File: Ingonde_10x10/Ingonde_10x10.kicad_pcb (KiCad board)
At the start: 2 copper layers, 100 x 100 mm, 738 parts, among them J1 2060-451/998-404, J10 2060-451/998-404, J100 Pastille, J101 Pastille, J102 Pastille, J103 Pastille, J104 Pastille, J105 Pastille, J106 Pastille, J107 Pastille, J108 Pastille, J109 Pastille, J11 2060-451/998-404, J110 Pastille, J111 Pastille, J112 Pastille, J113 Pastille, J114 Pastille, J115 Pastille, J116 Pastille, J117 Pastille, J118 Pastille, J119 Pastille, J12 2060-451/998-404, J120 Pastille, J121 Pastille, J122 Pastille, J123 Pastille, J124 Pastille, J125 Pastille, J126 Pastille, J127 Pastille, J128 Pastille, J129 Pastille, J13 2060-451/998-404, J130 Pastille, J131 Pastille, J132 Pastille, J133 Pastille, J134 Pastille, J135 Pastille, J136 Pastille, J137 Pastille, J138 Pastille, J139 Pastille, J14 2060-451/998-404, J140 Pastille, J141 Pastille, J142 Pastille, J143 Pastille, J144 Pastille, J145 Pastille, J146 Pastille, J147 Pastille, J148 Pastille, J149 Pastille, J15 2060-451/998-404, J150 Pastille, J151 Pastille, J152 Pastille, J153 Pastille, J154 Pastille, J155 Pastille, J156 Pastille, J157 Pastille, J158 Pastille, J159 Pastille, J16 2060-451/998-404, J160 Pastille, J161 Pastille, J162 Pastille, J163 Pastille, J164 Pastille, J165 Pastille, J166 Pastille, J167 Pastille, J168 Pastille, J169 Pastille, J17 2060-451/998-404, J170 Pastille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

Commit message: Ingonde 10x10 : passage à kicad 9.0.1
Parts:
- moved J33 2.54 mm to (141.1, 118.1)
- moved J48 2.54 mm to (179.2, 118.1)
- moved J51 2.54 mm to (186.8, 118.1)
- moved J20 2.54 mm to (108.1, 118.1)
- moved J22 2.54 mm to (113.2, 118.1)
- moved J24 2.54 mm to (118.2, 118.1)
- moved J25 2.54 mm to (120.8, 118.1)
- moved J27 2.54 mm to (125.9, 118.1)
- moved J19 2.54 mm to (105.5, 118.1)
- moved J21 2.54 mm to (110.6, 118.1)
- moved J23 2.54 mm to (115.7, 118.1)
- moved J26 2.54 mm to (123.3, 118.1)
- moved J34 2.54 mm to (143.7, 118.1)
- moved J38 2.54 mm to (153.8, 118.1)
- moved J39 2.54 mm to (156.3, 118.1)
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
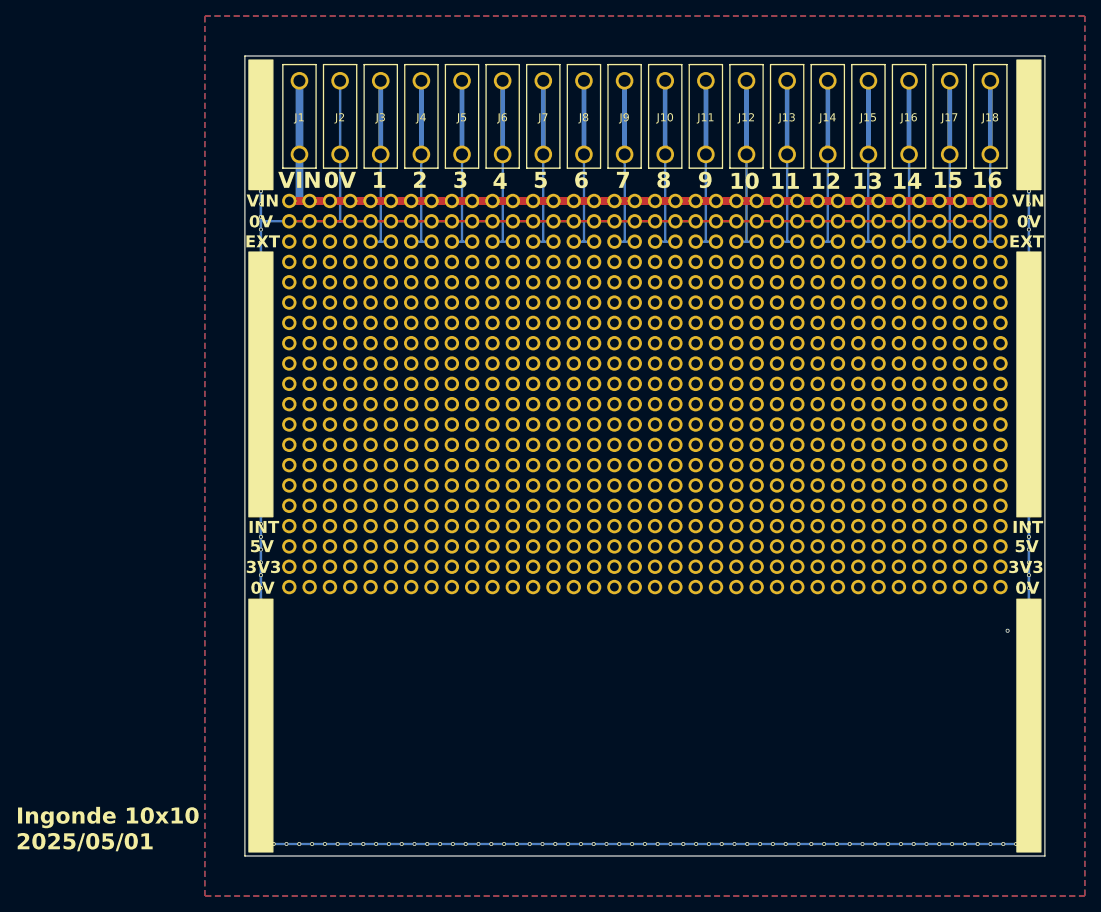
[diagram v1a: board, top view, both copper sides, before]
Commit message: Ingonde : fin matrice, pastille carrée, vias a 2,54mm
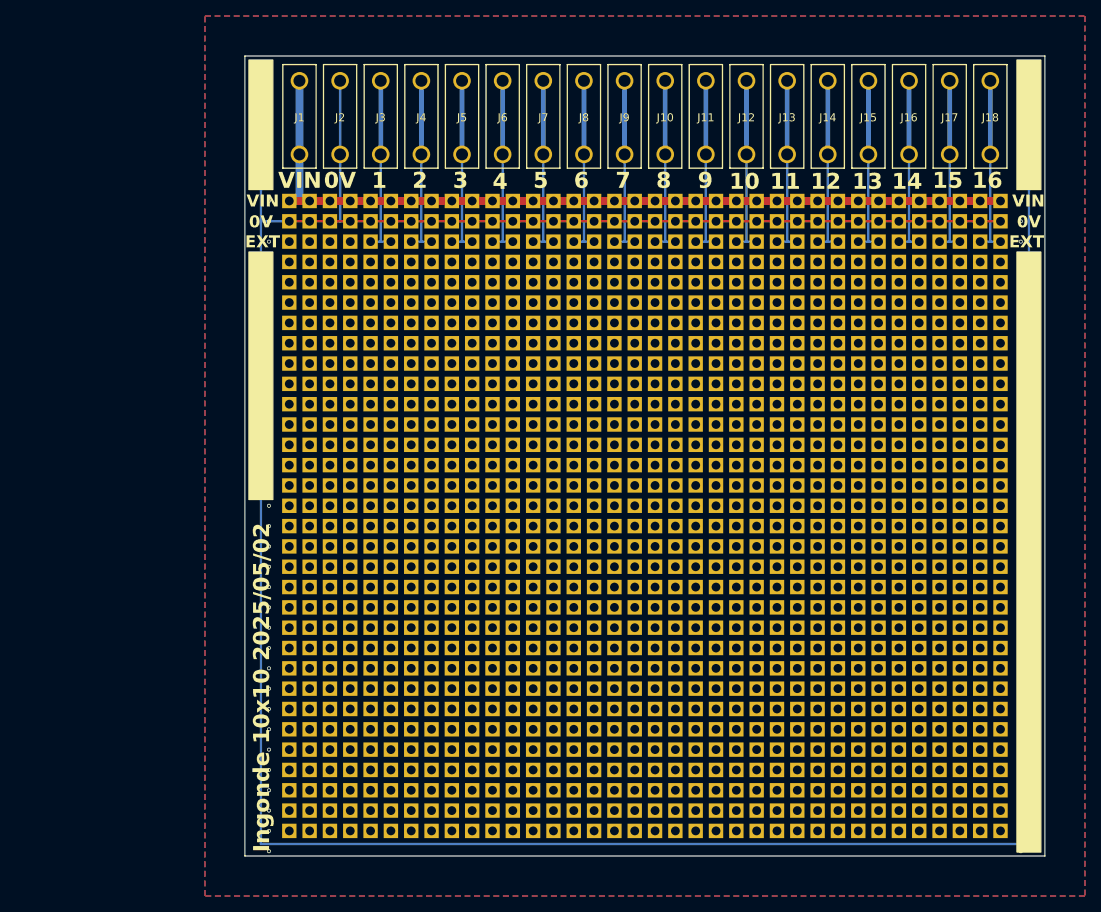
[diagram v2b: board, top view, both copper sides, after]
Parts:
- added J1000: Pastille, Chimere_comps:Pastille_carree, F.Cu at (125.9, 186.7)
- added J1001: Pastille, Chimere_comps:Pastille_carree, F.Cu at (128.4, 186.7)
- added J1002: Pastille, Chimere_comps:Pastille_carree, F.Cu at (130.9, 186.7)
- added J1003: Pastille, Chimere_comps:Pastille_carree, F.Cu at (133.5, 186.7)
- added J1004: Pastille, Chimere_comps:Pastille_carree, F.Cu at (136.0, 186.7)
- added J1005: Pastille, Chimere_comps:Pastille_carree, F.Cu at (138.6, 186.7)
- added J1006: Pastille, Chimere_comps:Pastille_carree, F.Cu at (141.1, 186.7)
- added J1007: Pastille, Chimere_comps:Pastille_carree, F.Cu at (143.7, 186.7)
- added J1008: Pastille, Chimere_comps:Pastille_carree, F.Cu at (146.2, 186.7)
- added J1009: Pastille, Chimere_comps:Pastille_carree, F.Cu at (148.7, 186.7)
- added J1010: Pastille, Chimere_comps:Pastille_carree, F.Cu at (151.3, 186.7)
- added J1011: Pastille, Chimere_comps:Pastille_carree, F.Cu at (153.8, 186.7)
- added J1012: Pastille, Chimere_comps:Pastille_carree, F.Cu at (156.3, 186.7)
- added J1013: Pastille, Chimere_comps:Pastille_carree, F.Cu at (158.9, 186.7)
- added J1014: Pastille, Chimere_comps:Pastille_carree, F.Cu at (161.4, 186.7)
- added J1015: Pastille, Chimere_comps:Pastille_carree, F.Cu at (164.0, 186.7)
- added J1016: Pastille, Chimere_comps:Pastille_carree, F.Cu at (166.5, 186.7)
- added J1017: Pastille, Chimere_comps:Pastille_carree, F.Cu at (169.1, 186.7)
- added J1018: Pastille, Chimere_comps:Pastille_carree, F.Cu at (171.6, 186.7)
- added J1019: Pastille, Chimere_comps:Pastille_carree, F.Cu at (174.1, 186.7)
- added J1020: Pastille, Chimere_comps:Pastille_carree, F.Cu at (176.7, 186.7)
- added J1021: Pastille, Chimere_comps:Pastille_carree, F.Cu at (179.2, 186.7)
- added J1022: Pastille, Chimere_comps:Pastille_carree, F.Cu at (181.8, 186.7)
- added J1023: Pastille, Chimere_comps:Pastille_carree, F.Cu at (184.3, 186.7)
- added J1024: Pastille, Chimere_comps:Pastille_carree, F.Cu at (186.8, 186.7)
- added J1025: Pastille, Chimere_comps:Pastille_carree, F.Cu at (189.4, 186.7)
- added J1026: Pastille, Chimere_comps:Pastille_carree, F.Cu at (191.9, 186.7)
- added J1027: Pastille, Chimere_comps:Pastille_carree, F.Cu at (194.4, 186.7)
- added J1028: Pastille, Chimere_comps:Pastille_carree, F.Cu at (105.5, 189.2)
- added J1029: Pastille, Chimere_comps:Pastille_carree, F.Cu at (108.1, 189.2)
- added J1030: Pastille, Chimere_comps:Pastille_carree, F.Cu at (110.6, 189.2)
- added J1031: Pastille, Chimere_comps:Pastille_carree, F.Cu at (113.2, 189.2)
- added J1032: Pastille, Chimere_comps:Pastille_carree, F.Cu at (115.7, 189.2)
- added J1033: Pastille, Chimere_comps:Pastille_carree, F.Cu at (118.2, 189.2)
- added J1034: Pastille, Chimere_comps:Pastille_carree, F.Cu at (120.8, 189.2)
- added J1035: Pastille, Chimere_comps:Pastille_carree, F.Cu at (123.3, 189.2)
- added J1036: Pastille, Chimere_comps:Pastille_carree, F.Cu at (125.9, 189.2)
- added J1037: Pastille, Chimere_comps:Pastille_carree, F.Cu at (128.4, 189.2)
- added J1038: Pastille, Chimere_comps:Pastille_carree, F.Cu at (130.9, 189.2)
- added J1039: Pastille, Chimere_comps:Pastille_carree, F.Cu at (133.5, 189.2)
- added J1040: Pastille, Chimere_comps:Pastille_carree, F.Cu at (136.0, 189.2)
- added J1041: Pastille, Chimere_comps:Pastille_carree, F.Cu at (138.6, 189.2)
- added J1042: Pastille, Chimere_comps:Pastille_carree, F.Cu at (141.1, 189.2)
- added J1043: Pastille, Chimere_comps:Pastille_carree, F.Cu at (143.7, 189.2)
- added J1044: Pastille, Chimere_comps:Pastille_carree, F.Cu at (146.2, 189.2)
- added J1045: Pastille, Chimere_comps:Pastille_carree, F.Cu at (148.7, 189.2)
- added J1046: Pastille, Chimere_comps:Pastille_carree, F.Cu at (151.3, 189.2)
- added J1047: Pastille, Chimere_comps:Pastille_carree, F.Cu at (153.8, 189.2)
- added J1048: Pastille, Chimere_comps:Pastille_carree, F.Cu at (156.3, 189.2)
- added J1049: Pastille, Chimere_comps:Pastille_carree, F.Cu at (158.9, 189.2)
- added J1050: Pastille, Chimere_comps:Pastille_carree, F.Cu at (161.4, 189.2)
- added J1051: Pastille, Chimere_comps:Pastille_carree, F.Cu at (164.0, 189.2)
- added J1052: Pastille, Chimere_comps:Pastille_carree, F.Cu at (166.5, 189.2)
- added J1053: Pastille, Chimere_comps:Pastille_carree, F.Cu at (169.1, 189.2)
- added J1054: Pastille, Chimere_comps:Pastille_carree, F.Cu at (171.6, 189.2)
- added J1055: Pastille, Chimere_comps:Pastille_carree, F.Cu at (174.1, 189.2)
- added J1056: Pastille, Chimere_comps:Pastille_carree, F.Cu at (176.7, 189.2)
- added J1057: Pastille, Chimere_comps:Pastille_carree, F.Cu at (179.2, 189.2)
- added J1058: Pastille, Chimere_comps:Pastille_carree, F.Cu at (181.8, 189.2)
- added J1059: Pastille, Chimere_comps:Pastille_carree, F.Cu at (184.3, 189.2)
- added J1060: Pastille, Chimere_comps:Pastille_carree, F.Cu at (186.8, 189.2)
- added J1061: Pastille, Chimere_comps:Pastille_carree, F.Cu at (189.4, 189.2)
- added J1062: Pastille, Chimere_comps:Pastille_carree, F.Cu at (191.9, 189.2)
- added J1063: Pastille, Chimere_comps:Pastille_carree, F.Cu at (194.4, 189.2)
- added J1064: Pastille, Chimere_comps:Pastille_carree, F.Cu at (105.5, 191.8)
- added J1065: Pastille, Chimere_comps:Pastille_carree, F.Cu at (108.1, 191.8)
- added J1066: Pastille, Chimere_comps:Pastille_carree, F.Cu at (110.6, 191.8)
- added J1067: Pastille, Chimere_comps:Pastille_carree, F.Cu at (113.2, 191.8)
- added J1068: Pastille, Chimere_comps:Pastille_carree, F.Cu at (115.7, 191.8)
- added J1069: Pastille, Chimere_comps:Pastille_carree, F.Cu at (118.2, 191.8)
- added J1070: Pastille, Chimere_comps:Pastille_carree, F.Cu at (120.8, 191.8)
- added J1071: Pastille, Chimere_comps:Pastille_carree, F.Cu at (123.3, 191.8)
- added J1072: Pastille, Chimere_comps:Pastille_carree, F.Cu at (125.9, 191.8)
- added J1073: Pastille, Chimere_comps:Pastille_carree, F.Cu at (128.4, 191.8)
- added J1074: Pastille, Chimere_comps:Pastille_carree, F.Cu at (130.9, 191.8)
- added J1075: Pastille, Chimere_comps:Pastille_carree, F.Cu at (133.5, 191.8)
- added J1076: Pastille, Chimere_comps:Pastille_carree, F.Cu at (136.0, 191.8)
- added J1077: Pastille, Chimere_comps:Pastille_carree, F.Cu at (138.6, 191.8)
- added J1078: Pastille, Chimere_comps:Pastille_carree, F.Cu at (141.1, 191.8)
- added J1079: Pastille, Chimere_comps:Pastille_carree, F.Cu at (143.7, 191.8)
- added J1080: Pastille, Chimere_comps:Pastille_carree, F.Cu at (146.2, 191.8)
- added J1081: Pastille, Chimere_comps:Pastille_carree, F.Cu at (148.7, 191.8)
- added J1082: Pastille, Chimere_comps:Pastille_carree, F.Cu at (151.3, 191.8)
- added J1083: Pastille, Chimere_comps:Pastille_carree, F.Cu at (153.8, 191.8)
- added J1084: Pastille, Chimere_comps:Pastille_carree, F.Cu at (156.3, 191.8)
- added J1085: Pastille, Chimere_comps:Pastille_carree, F.Cu at (158.9, 191.8)
- added J1086: Pastille, Chimere_comps:Pastille_carree, F.Cu at (161.4, 191.8)
- added J1087: Pastille, Chimere_comps:Pastille_carree, F.Cu at (164.0, 191.8)
- added J1088: Pastille, Chimere_comps:Pastille_carree, F.Cu at (166.5, 191.8)
- added J1089: Pastille, Chimere_comps:Pastille_carree, F.Cu at (169.1, 191.8)
- added J1090: Pastille, Chimere_comps:Pastille_carree, F.Cu at (171.6, 191.8)
- added J1091: Pastille, Chimere_comps:Pastille_carree, F.Cu at (174.1, 191.8)
- added J1092: Pastille, Chimere_comps:Pastille_carree, F.Cu at (176.7, 191.8)
- added J1093: Pastille, Chimere_comps:Pastille_carree, F.Cu at (179.2, 191.8)
- added J1094: Pastille, Chimere_comps:Pastille_carree, F.Cu at (181.8, 191.8)
- added J1095: Pastille, Chimere_comps:Pastille_carree, F.Cu at (184.3, 191.8)
- added J1096: Pastille, Chimere_comps:Pastille_carree, F.Cu at (186.8, 191.8)
- added J1097: Pastille, Chimere_comps:Pastille_carree, F.Cu at (189.4, 191.8)
- added J1098: Pastille, Chimere_comps:Pastille_carree, F.Cu at (191.9, 191.8)
- added J1099: Pastille, Chimere_comps:Pastille_carree, F.Cu at (194.4, 191.8)
- added J1100: Pastille, Chimere_comps:Pastille_carree, F.Cu at (105.5, 194.3)
- added J1101: Pastille, Chimere_comps:Pastille_carree, F.Cu at (108.1, 194.3)
- added J1102: Pastille, Chimere_comps:Pastille_carree, F.Cu at (110.6, 194.3)
- added J1103: Pastille, Chimere_comps:Pastille_carree, F.Cu at (113.2, 194.3)
- added J1104: Pastille, Chimere_comps:Pastille_carree, F.Cu at (115.7, 194.3)
- added J1105: Pastille, Chimere_comps:Pastille_carree, F.Cu at (118.2, 194.3)
- added J1106: Pastille, Chimere_comps:Pastille_carree, F.Cu at (120.8, 194.3)
- added J1107: Pastille, Chimere_comps:Pastille_carree, F.Cu at (123.3, 194.3)
- added J1108: Pastille, Chimere_comps:Pastille_carree, F.Cu at (125.9, 194.3)
- added J1109: Pastille, Chimere_comps:Pastille_carree, F.Cu at (128.4, 194.3)
- added J1110: Pastille, Chimere_comps:Pastille_carree, F.Cu at (130.9, 194.3)
- added J1111: Pastille, Chimere_comps:Pastille_carree, F.Cu at (133.5, 194.3)
- added J1112: Pastille, Chimere_comps:Pastille_carree, F.Cu at (136.0, 194.3)
- added J1113: Pastille, Chimere_comps:Pastille_carree, F.Cu at (138.6, 194.3)
- added J1114: Pastille, Chimere_comps:Pastille_carree, F.Cu at (141.1, 194.3)
- added J1115: Pastille, Chimere_comps:Pastille_carree, F.Cu at (143.7, 194.3)
- added J1116: Pastille, Chimere_comps:Pastille_carree, F.Cu at (146.2, 194.3)
- added J1117: Pastille, Chimere_comps:Pastille_carree, F.Cu at (148.7, 194.3)
- added J1118: Pastille, Chimere_comps:Pastille_carree, F.Cu at (151.3, 194.3)
- added J1119: Pastille, Chimere_comps:Pastille_carree, F.Cu at (153.8, 194.3)
- added J1120: Pastille, Chimere_comps:Pastille_carree, F.Cu at (156.3, 194.3)
- added J1121: Pastille, Chimere_comps:Pastille_carree, F.Cu at (158.9, 194.3)
- added J1122: Pastille, Chimere_comps:Pastille_carree, F.Cu at (161.4, 194.3)
- added J1123: Pastille, Chimere_comps:Pastille_carree, F.Cu at (164.0, 194.3)
- added J1124: Pastille, Chimere_comps:Pastille_carree, F.Cu at (166.5, 194.3)
- added J1125: Pastille, Chimere_comps:Pastille_carree, F.Cu at (169.1, 194.3)
- added J1126: Pastille, Chimere_comps:Pastille_carree, F.Cu at (171.6, 194.3)
- added J1127: Pastille, Chimere_comps:Pastille_carree, F.Cu at (174.1, 194.3)
- added J1128: Pastille, Chimere_comps:Pastille_carree, F.Cu at (176.7, 194.3)
- added J1129: Pastille, Chimere_comps:Pastille_carree, F.Cu at (179.2, 194.3)
- added J1130: Pastille, Chimere_comps:Pastille_carree, F.Cu at (181.8, 194.3)
- added J1131: Pastille, Chimere_comps:Pastille_carree, F.Cu at (184.3, 194.3)
- added J1132: Pastille, Chimere_comps:Pastille_carree, F.Cu at (186.8, 194.3)
- added J1133: Pastille, Chimere_comps:Pastille_carree, F.Cu at (189.4, 194.3)
- added J1134: Pastille, Chimere_comps:Pastille_carree, F.Cu at (191.9, 194.3)
- added J1135: Pastille, Chimere_comps:Pastille_carree, F.Cu at (194.4, 196.9)
- added J1136: Pastille, Chimere_comps:Pastille_carree, F.Cu at (105.5, 196.9)
- added J1137: Pastille, Chimere_comps:Pastille_carree, F.Cu at (108.1, 196.9)
- added J1138: Pastille, Chimere_comps:Pastille_carree, F.Cu at (110.6, 196.9)
- added J1139: Pastille, Chimere_comps:Pastille_carree, F.Cu at (113.2, 196.9)
- added J1140: Pastille, Chimere_comps:Pastille_carree, F.Cu at (115.7, 196.9)
- added J1141: Pastille, Chimere_comps:Pastille_carree, F.Cu at (118.2, 196.9)
- added J1142: Pastille, Chimere_comps:Pastille_carree, F.Cu at (120.8, 196.9)
- added J1143: Pastille, Chimere_comps:Pastille_carree, F.Cu at (123.3, 196.9)
- added J1144: Pastille, Chimere_comps:Pastille_carree, F.Cu at (125.9, 196.9)
- added J1145: Pastille, Chimere_comps:Pastille_carree, F.Cu at (128.4, 196.9)
- added J1146: Pastille, Chimere_comps:Pastille_carree, F.Cu at (130.9, 196.9)
- added J1147: Pastille, Chimere_comps:Pastille_carree, F.Cu at (133.5, 196.9)
- added J1148: Pastille, Chimere_comps:Pastille_carree, F.Cu at (136.0, 196.9)
- added J1149: Pastille, Chimere_comps:Pastille_carree, F.Cu at (138.6, 196.9)
- added J1150: Pastille, Chimere_comps:Pastille_carree, F.Cu at (141.1, 196.9)
- added J1151: Pastille, Chimere_comps:Pastille_carree, F.Cu at (143.7, 196.9)
- added J1152: Pastille, Chimere_comps:Pastille_carree, F.Cu at (146.2, 196.9)
- added J1153: Pastille, Chimere_comps:Pastille_carree, F.Cu at (148.7, 196.9)
- added J1154: Pastille, Chimere_comps:Pastille_carree, F.Cu at (151.3, 196.9)
- added J1155: Pastille, Chimere_comps:Pastille_carree, F.Cu at (153.8, 196.9)
- added J1156: Pastille, Chimere_comps:Pastille_carree, F.Cu at (156.3, 196.9)
- added J1157: Pastille, Chimere_comps:Pastille_carree, F.Cu at (158.9, 196.9)
- added J1158: Pastille, Chimere_comps:Pastille_carree, F.Cu at (161.4, 196.9)
- added J1159: Pastille, Chimere_comps:Pastille_carree, F.Cu at (164.0, 196.9)
- added J1160: Pastille, Chimere_comps:Pastille_carree, F.Cu at (166.5, 196.9)
- added J1161: Pastille, Chimere_comps:Pastille_carree, F.Cu at (169.1, 196.9)
- added J1162: Pastille, Chimere_comps:Pastille_carree, F.Cu at (171.6, 196.9)
- added J1163: Pastille, Chimere_comps:Pastille_carree, F.Cu at (174.1, 196.9)
- added J1164: Pastille, Chimere_comps:Pastille_carree, F.Cu at (176.7, 196.9)
- added J1165: Pastille, Chimere_comps:Pastille_carree, F.Cu at (179.2, 196.9)
- added J1166: Pastille, Chimere_comps:Pastille_carree, F.Cu at (181.8, 196.9)
- added J1167: Pastille, Chimere_comps:Pastille_carree, F.Cu at (184.3, 196.9)
- added J1168: Pastille, Chimere_comps:Pastille_carree, F.Cu at (186.8, 196.9)
- added J1169: Pastille, Chimere_comps:Pastille_carree, F.Cu at (189.4, 196.9)
- added J1170: Pastille, Chimere_comps:Pastille_carree, F.Cu at (191.9, 196.9)
- added J739: Pastille, Chimere_comps:Pastille_carree, F.Cu at (194.4, 184.2)
- added J740: Pastille, Chimere_comps:Pastille_carree, F.Cu at (105.5, 168.9)
- added J741: Pastille, Chimere_comps:Pastille_carree, F.Cu at (108.1, 168.9)
- added J742: Pastille, Chimere_comps:Pastille_carree, F.Cu at (110.6, 168.9)
- added J743: Pastille, Chimere_comps:Pastille_carree, F.Cu at (113.2, 168.9)
- added J744: Pastille, Chimere_comps:Pastille_carree, F.Cu at (115.7, 168.9)
- added J745: Pastille, Chimere_comps:Pastille_carree, F.Cu at (118.2, 168.9)
- added J746: Pastille, Chimere_comps:Pastille_carree, F.Cu at (120.8, 168.9)
- added J747: Pastille, Chimere_comps:Pastille_carree, F.Cu at (123.3, 168.9)
- added J748: Pastille, Chimere_comps:Pastille_carree, F.Cu at (125.9, 168.9)
- added J749: Pastille, Chimere_comps:Pastille_carree, F.Cu at (128.4, 168.9)
- added J750: Pastille, Chimere_comps:Pastille_carree, F.Cu at (130.9, 168.9)
- added J751: Pastille, Chimere_comps:Pastille_carree, F.Cu at (133.5, 168.9)
- added J752: Pastille, Chimere_comps:Pastille_carree, F.Cu at (136.0, 168.9)
- added J753: Pastille, Chimere_comps:Pastille_carree, F.Cu at (138.6, 168.9)
- added J754: Pastille, Chimere_comps:Pastille_carree, F.Cu at (141.1, 168.9)
- added J755: Pastille, Chimere_comps:Pastille_carree, F.Cu at (143.7, 168.9)
- added J756: Pastille, Chimere_comps:Pastille_carree, F.Cu at (146.2, 168.9)
- added J757: Pastille, Chimere_comps:Pastille_carree, F.Cu at (148.7, 168.9)
- added J758: Pastille, Chimere_comps:Pastille_carree, F.Cu at (151.3, 168.9)
- added J759: Pastille, Chimere_comps:Pastille_carree, F.Cu at (153.8, 168.9)
- added J760: Pastille, Chimere_comps:Pastille_carree, F.Cu at (156.3, 168.9)
- added J761: Pastille, Chimere_comps:Pastille_carree, F.Cu at (158.9, 168.9)
- added J762: Pastille, Chimere_comps:Pastille_carree, F.Cu at (161.4, 168.9)
- added J763: Pastille, Chimere_comps:Pastille_carree, F.Cu at (164.0, 168.9)
- added J764: Pastille, Chimere_comps:Pastille_carree, F.Cu at (166.5, 168.9)
- added J765: Pastille, Chimere_comps:Pastille_carree, F.Cu at (169.1, 168.9)
- added J766: Pastille, Chimere_comps:Pastille_carree, F.Cu at (171.6, 168.9)
- added J767: Pastille, Chimere_comps:Pastille_carree, F.Cu at (174.1, 168.9)
- added J768: Pastille, Chimere_comps:Pastille_carree, F.Cu at (176.7, 168.9)
- added J769: Pastille, Chimere_comps:Pastille_carree, F.Cu at (179.2, 168.9)
- added J770: Pastille, Chimere_comps:Pastille_carree, F.Cu at (181.8, 168.9)
- added J771: Pastille, Chimere_comps:Pastille_carree, F.Cu at (184.3, 168.9)
- added J772: Pastille, Chimere_comps:Pastille_carree, F.Cu at (186.8, 168.9)
- added J773: Pastille, Chimere_comps:Pastille_carree, F.Cu at (189.4, 168.9)
- added J774: Pastille, Chimere_comps:Pastille_carree, F.Cu at (191.9, 168.9)
- added J775: Pastille, Chimere_comps:Pastille_carree, F.Cu at (194.4, 168.9)
- added J776: Pastille, Chimere_comps:Pastille_carree, F.Cu at (105.5, 171.5)
- added J777: Pastille, Chimere_comps:Pastille_carree, F.Cu at (108.1, 171.5)
- added J778: Pastille, Chimere_comps:Pastille_carree, F.Cu at (110.6, 171.5)
- added J779: Pastille, Chimere_comps:Pastille_carree, F.Cu at (113.2, 171.5)
- added J780: Pastille, Chimere_comps:Pastille_carree, F.Cu at (115.7, 171.5)
- added J781: Pastille, Chimere_comps:Pastille_carree, F.Cu at (118.2, 171.5)
- added J782: Pastille, Chimere_comps:Pastille_carree, F.Cu at (120.8, 171.5)
- added J783: Pastille, Chimere_comps:Pastille_carree, F.Cu at (123.3, 171.5)
- added J784: Pastille, Chimere_comps:Pastille_carree, F.Cu at (125.9, 171.5)
- added J785: Pastille, Chimere_comps:Pastille_carree, F.Cu at (128.4, 171.5)
- added J786: Pastille, Chimere_comps:Pastille_carree, F.Cu at (130.9, 171.5)
- added J787: Pastille, Chimere_comps:Pastille_carree, F.Cu at (133.5, 171.5)
- added J788: Pastille, Chimere_comps:Pastille_carree, F.Cu at (136.0, 171.5)
- added J789: Pastille, Chimere_comps:Pastille_carree, F.Cu at (138.6, 171.5)
- added J790: Pastille, Chimere_comps:Pastille_carree, F.Cu at (141.1, 171.5)
- added J791: Pastille, Chimere_comps:Pastille_carree, F.Cu at (143.7, 171.5)
- added J792: Pastille, Chimere_comps:Pastille_carree, F.Cu at (146.2, 171.5)
- added J793: Pastille, Chimere_comps:Pastille_carree, F.Cu at (148.7, 171.5)
- added J794: Pastille, Chimere_comps:Pastille_carree, F.Cu at (151.3, 171.5)
- added J795: Pastille, Chimere_comps:Pastille_carree, F.Cu at (153.8, 171.5)
- added J796: Pastille, Chimere_comps:Pastille_carree, F.Cu at (156.3, 171.5)
- added J797: Pastille, Chimere_comps:Pastille_carree, F.Cu at (158.9, 171.5)
- added J798: Pastille, Chimere_comps:Pastille_carree, F.Cu at (161.4, 171.5)
- added J799: Pastille, Chimere_comps:Pastille_carree, F.Cu at (164.0, 171.5)
- added J800: Pastille, Chimere_comps:Pastille_carree, F.Cu at (166.5, 171.5)
- added J801: Pastille, Chimere_comps:Pastille_carree, F.Cu at (169.1, 171.5)
- added J802: Pastille, Chimere_comps:Pastille_carree, F.Cu at (171.6, 171.5)
- added J803: Pastille, Chimere_comps:Pastille_carree, F.Cu at (174.1, 171.5)
- added J804: Pastille, Chimere_comps:Pastille_carree, F.Cu at (176.7, 171.5)
- added J805: Pastille, Chimere_comps:Pastille_carree, F.Cu at (179.2, 171.5)
- added J806: Pastille, Chimere_comps:Pastille_carree, F.Cu at (181.8, 171.5)
- added J807: Pastille, Chimere_comps:Pastille_carree, F.Cu at (184.3, 171.5)
- added J808: Pastille, Chimere_comps:Pastille_carree, F.Cu at (186.8, 171.5)
- added J809: Pastille, Chimere_comps:Pastille_carree, F.Cu at (189.4, 171.5)
- added J810: Pastille, Chimere_comps:Pastille_carree, F.Cu at (191.9, 171.5)
- added J811: Pastille, Chimere_comps:Pastille_carree, F.Cu at (194.4, 171.5)
- added J812: Pastille, Chimere_comps:Pastille_carree, F.Cu at (105.5, 174.0)
- added J813: Pastille, Chimere_comps:Pastille_carree, F.Cu at (108.1, 174.0)
- added J814: Pastille, Chimere_comps:Pastille_carree, F.Cu at (110.6, 174.0)
- added J815: Pastille, Chimere_comps:Pastille_carree, F.Cu at (113.2, 174.0)
- added J816: Pastille, Chimere_comps:Pastille_carree, F.Cu at (115.7, 174.0)
- added J817: Pastille, Chimere_comps:Pastille_carree, F.Cu at (118.2, 174.0)
- added J818: Pastille, Chimere_comps:Pastille_carree, F.Cu at (120.8, 174.0)
- added J819: Pastille, Chimere_comps:Pastille_carree, F.Cu at (123.3, 174.0)
- added J820: Pastille, Chimere_comps:Pastille_carree, F.Cu at (125.9, 174.0)
- added J821: Pastille, Chimere_comps:Pastille_carree, F.Cu at (128.4, 174.0)
- added J822: Pastille, Chimere_comps:Pastille_carree, F.Cu at (130.9, 174.0)
- added J823: Pastille, Chimere_comps:Pastille_carree, F.Cu at (133.5, 174.0)
- added J824: Pastille, Chimere_comps:Pastille_carree, F.Cu at (136.0, 174.0)
- added J825: Pastille, Chimere_comps:Pastille_carree, F.Cu at (138.6, 174.0)
- added J826: Pastille, Chimere_comps:Pastille_carree, F.Cu at (141.1, 174.0)
- added J827: Pastille, Chimere_comps:Pastille_carree, F.Cu at (143.7, 174.0)
- added J828: Pastille, Chimere_comps:Pastille_carree, F.Cu at (146.2, 174.0)
- added J829: Pastille, Chimere_comps:Pastille_carree, F.Cu at (148.7, 174.0)
- added J830: Pastille, Chimere_comps:Pastille_carree, F.Cu at (151.3, 174.0)
- added J831: Pastille, Chimere_comps:Pastille_carree, F.Cu at (153.8, 174.0)
- added J832: Pastille, Chimere_comps:Pastille_carree, F.Cu at (156.3, 174.0)
- added J833: Pastille, Chimere_comps:Pastille_carree, F.Cu at (158.9, 174.0)
- added J834: Pastille, Chimere_comps:Pastille_carree, F.Cu at (161.4, 174.0)
- added J835: Pastille, Chimere_comps:Pastille_carree, F.Cu at (164.0, 174.0)
- added J836: Pastille, Chimere_comps:Pastille_carree, F.Cu at (166.5, 174.0)
- added J837: Pastille, Chimere_comps:Pastille_carree, F.Cu at (169.1, 174.0)
- added J838: Pastille, Chimere_comps:Pastille_carree, F.Cu at (171.6, 174.0)
- added J839: Pastille, Chimere_comps:Pastille_carree, F.Cu at (174.1, 174.0)
- added J840: Pastille, Chimere_comps:Pastille_carree, F.Cu at (176.7, 174.0)
- added J841: Pastille, Chimere_comps:Pastille_carree, F.Cu at (179.2, 174.0)
- added J842: Pastille, Chimere_comps:Pastille_carree, F.Cu at (181.8, 174.0)
- added J843: Pastille, Chimere_comps:Pastille_carree, F.Cu at (184.3, 174.0)
- added J844: Pastille, Chimere_comps:Pastille_carree, F.Cu at (186.8, 174.0)
- added J845: Pastille, Chimere_comps:Pastille_carree, F.Cu at (189.4, 174.0)
- added J846: Pastille, Chimere_comps:Pastille_carree, F.Cu at (191.9, 174.0)
- added J847: Pastille, Chimere_comps:Pastille_carree, F.Cu at (194.4, 174.0)
- added J848: Pastille, Chimere_comps:Pastille_carree, F.Cu at (105.5, 176.5)
- added J849: Pastille, Chimere_comps:Pastille_carree, F.Cu at (108.1, 176.5)
- added J850: Pastille, Chimere_comps:Pastille_carree, F.Cu at (110.6, 176.5)
- added J851: Pastille, Chimere_comps:Pastille_carree, F.Cu at (113.2, 176.5)
- added J852: Pastille, Chimere_comps:Pastille_carree, F.Cu at (115.7, 176.5)
- added J853: Pastille, Chimere_comps:Pastille_carree, F.Cu at (118.2, 176.5)
- added J854: Pastille, Chimere_comps:Pastille_carree, F.Cu at (120.8, 176.5)
- added J855: Pastille, Chimere_comps:Pastille_carree, F.Cu at (123.3, 176.5)
- added J856: Pastille, Chimere_comps:Pastille_carree, F.Cu at (125.9, 176.5)
- added J857: Pastille, Chimere_comps:Pastille_carree, F.Cu at (128.4, 176.5)
- added J858: Pastille, Chimere_comps:Pastille_carree, F.Cu at (130.9, 176.5)
- added J859: Pastille, Chimere_comps:Pastille_carree, F.Cu at (133.5, 176.5)
- added J860: Pastille, Chimere_comps:Pastille_carree, F.Cu at (136.0, 176.5)
- added J861: Pastille, Chimere_comps:Pastille_carree, F.Cu at (138.6, 176.5)
- added J862: Pastille, Chimere_comps:Pastille_carree, F.Cu at (141.1, 176.5)
- added J863: Pastille, Chimere_comps:Pastille_carree, F.Cu at (143.7, 176.5)
- added J864: Pastille, Chimere_comps:Pastille_carree, F.Cu at (146.2, 176.5)
- added J865: Pastille, Chimere_comps:Pastille_carree, F.Cu at (148.7, 176.5)
- added J866: Pastille, Chimere_comps:Pastille_carree, F.Cu at (151.3, 176.5)
- added J867: Pastille, Chimere_comps:Pastille_carree, F.Cu at (153.8, 176.5)
- added J868: Pastille, Chimere_comps:Pastille_carree, F.Cu at (156.3, 176.5)
- added J869: Pastille, Chimere_comps:Pastille_carree, F.Cu at (158.9, 176.5)
- added J870: Pastille, Chimere_comps:Pastille_carree, F.Cu at (161.4, 176.5)
- added J871: Pastille, Chimere_comps:Pastille_carree, F.Cu at (164.0, 176.5)
- added J872: Pastille, Chimere_comps:Pastille_carree, F.Cu at (166.5, 176.5)
- added J873: Pastille, Chimere_comps:Pastille_carree, F.Cu at (169.1, 176.5)
- added J874: Pastille, Chimere_comps:Pastille_carree, F.Cu at (171.6, 176.5)
- added J875: Pastille, Chimere_comps:Pastille_carree, F.Cu at (174.1, 176.5)
- added J876: Pastille, Chimere_comps:Pastille_carree, F.Cu at (176.7, 176.5)
- added J877: Pastille, Chimere_comps:Pastille_carree, F.Cu at (179.2, 176.5)
- added J878: Pastille, Chimere_comps:Pastille_carree, F.Cu at (181.8, 176.5)
- added J879: Pastille, Chimere_comps:Pastille_carree, F.Cu at (184.3, 176.5)
- added J880: Pastille, Chimere_comps:Pastille_carree, F.Cu at (186.8, 176.5)
- added J881: Pastille, Chimere_comps:Pastille_carree, F.Cu at (189.4, 176.5)
- added J882: Pastille, Chimere_comps:Pastille_carree, F.Cu at (191.9, 176.5)
- added J883: Pastille, Chimere_comps:Pastille_carree, F.Cu at (194.4, 176.5)
- added J884: Pastille, Chimere_comps:Pastille_carree, F.Cu at (105.5, 179.1)
- added J885: Pastille, Chimere_comps:Pastille_carree, F.Cu at (108.1, 179.1)
- added J886: Pastille, Chimere_comps:Pastille_carree, F.Cu at (110.6, 179.1)
- added J887: Pastille, Chimere_comps:Pastille_carree, F.Cu at (113.2, 179.1)
- added J888: Pastille, Chimere_comps:Pastille_carree, F.Cu at (115.7, 179.1)
- added J889: Pastille, Chimere_comps:Pastille_carree, F.Cu at (118.2, 179.1)
- added J890: Pastille, Chimere_comps:Pastille_carree, F.Cu at (120.8, 179.1)
- added J891: Pastille, Chimere_comps:Pastille_carree, F.Cu at (123.3, 179.1)
- added J892: Pastille, Chimere_comps:Pastille_carree, F.Cu at (125.9, 179.1)
- added J893: Pastille, Chimere_comps:Pastille_carree, F.Cu at (128.4, 179.1)
- added J894: Pastille, Chimere_comps:Pastille_carree, F.Cu at (130.9, 179.1)
- added J895: Pastille, Chimere_comps:Pastille_carree, F.Cu at (133.5, 179.1)
- added J896: Pastille, Chimere_comps:Pastille_carree, F.Cu at (136.0, 179.1)
- added J897: Pastille, Chimere_comps:Pastille_carree, F.Cu at (138.6, 179.1)
- added J898: Pastille, Chimere_comps:Pastille_carree, F.Cu at (141.1, 179.1)
- added J899: Pastille, Chimere_comps:Pastille_carree, F.Cu at (143.7, 179.1)
- added J900: Pastille, Chimere_comps:Pastille_carree, F.Cu at (146.2, 179.1)
- added J901: Pastille, Chimere_comps:Pastille_carree, F.Cu at (148.7, 179.1)
- added J902: Pastille, Chimere_comps:Pastille_carree, F.Cu at (151.3, 179.1)
- added J903: Pastille, Chimere_comps:Pastille_carree, F.Cu at (153.8, 179.1)
- added J904: Pastille, Chimere_comps:Pastille_carree, F.Cu at (156.3, 179.1)
- added J905: Pastille, Chimere_comps:Pastille_carree, F.Cu at (158.9, 179.1)
- added J906: Pastille, Chimere_comps:Pastille_carree, F.Cu at (161.4, 179.1)
- added J907: Pastille, Chimere_comps:Pastille_carree, F.Cu at (164.0, 179.1)
- added J908: Pastille, Chimere_comps:Pastille_carree, F.Cu at (166.5, 179.1)
- added J909: Pastille, Chimere_comps:Pastille_carree, F.Cu at (169.1, 179.1)
- added J910: Pastille, Chimere_comps:Pastille_carree, F.Cu at (171.6, 179.1)
- added J911: Pastille, Chimere_comps:Pastille_carree, F.Cu at (174.1, 179.1)
- added J912: Pastille, Chimere_comps:Pastille_carree, F.Cu at (176.7, 179.1)
- added J913: Pastille, Chimere_comps:Pastille_carree, F.Cu at (179.2, 179.1)
- added J914: Pastille, Chimere_comps:Pastille_carree, F.Cu at (181.8, 179.1)
- added J915: Pastille, Chimere_comps:Pastille_carree, F.Cu at (184.3, 179.1)
- added J916: Pastille, Chimere_comps:Pastille_carree, F.Cu at (186.8, 179.1)
- added J917: Pastille, Chimere_comps:Pastille_carree, F.Cu at (189.4, 179.1)
- added J918: Pastille, Chimere_comps:Pastille_carree, F.Cu at (191.9, 179.1)
- added J919: Pastille, Chimere_comps:Pastille_carree, F.Cu at (194.4, 179.1)
- added J920: Pastille, Chimere_comps:Pastille_carree, F.Cu at (105.5, 181.6)
- added J921: Pastille, Chimere_comps:Pastille_carree, F.Cu at (108.1, 181.6)
- added J922: Pastille, Chimere_comps:Pastille_carree, F.Cu at (110.6, 181.6)
- added J923: Pastille, Chimere_comps:Pastille_carree, F.Cu at (113.2, 181.6)
- added J924: Pastille, Chimere_comps:Pastille_carree, F.Cu at (115.7, 181.6)
- added J925: Pastille, Chimere_comps:Pastille_carree, F.Cu at (118.2, 181.6)
- added J926: Pastille, Chimere_comps:Pastille_carree, F.Cu at (120.8, 181.6)
- added J927: Pastille, Chimere_comps:Pastille_carree, F.Cu at (123.3, 181.6)
- added J928: Pastille, Chimere_comps:Pastille_carree, F.Cu at (125.9, 181.6)
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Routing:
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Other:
- board text added: "Ingonde 10x10 2025/05/02"
- board text removed: "3V3"
- board text removed: "5V"
- board text removed: "INT"
- board text removed: "Ingonde 10x10 2025/05/01"

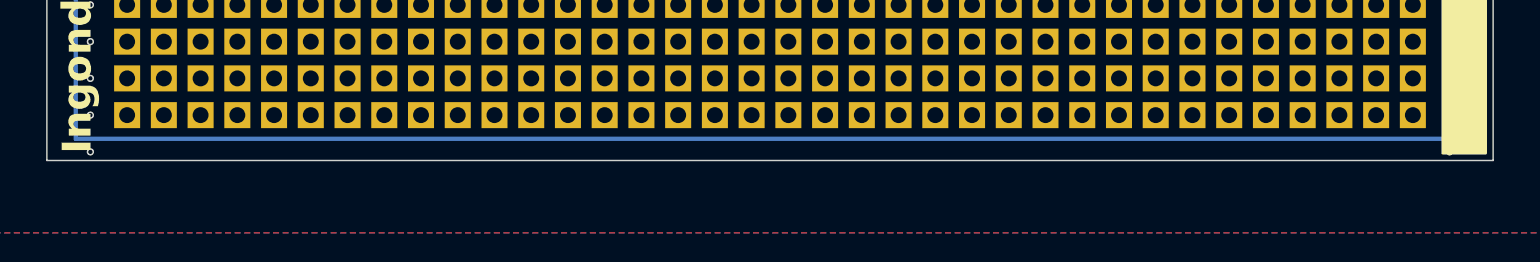
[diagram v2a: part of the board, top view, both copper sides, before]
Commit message: Ingonde_10x10 : moins de vias
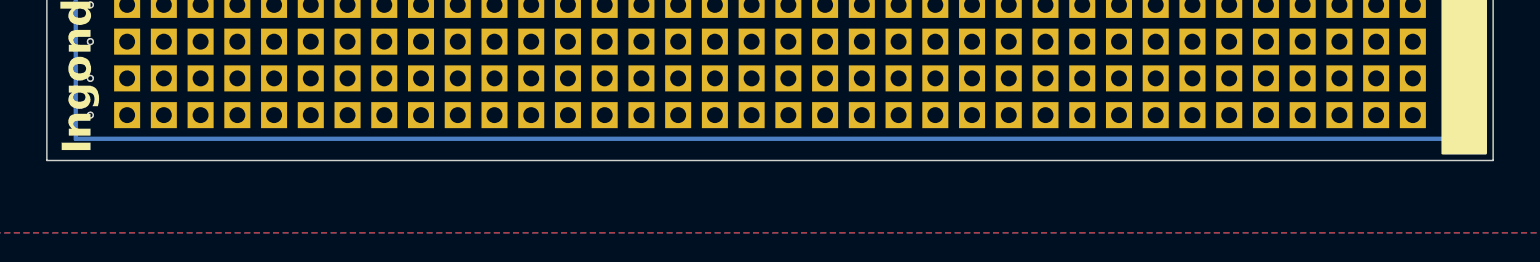
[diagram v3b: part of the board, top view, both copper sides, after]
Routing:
- net 0V: vias 78 -> 76
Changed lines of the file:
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@@
-	)
-	(via
-		(at 103.01 199.403)
-		(size 0.5)
-		(drill 0.3)
-		(layers "F.Cu" "B.Cu")
-		(net 2)
 	)
 	(via
@@
 		(net 2)
 	)
-	(via
-		(at 196.99 199.403)
-		(size 0.5)
-		(drill 0.3)
-		(layers "F.Cu" "B.Cu")
-		(free yes)
-		(net 2)
-	)

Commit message: Ingonde_10x10: doublage des connecteurs
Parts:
- J1: footprint Chimere_comps:CONN_2060-1451_998-404_WAGO -> Chimere_comps:Conn_bornier_et_wago
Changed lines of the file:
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@@
 		(embedded_fonts no)
 	)
-	(footprint "Chimere_comps:CONN_2060-1451_998-404_WAGO"
+	(footprint "Chimere_comps:Conn_bornier_et_wago"
 		(layer "F.Cu")
 		(at 106.82 112.3)
@@
 		)
 		(pad "1" thru_hole circle
+			(at 0 -6.9)
+			(size 2.2 2.2)
+			(drill 1.4986)
+			(layers "*.Cu" "*.Mask")
+			(remove_unused_layers no)
+			(net 1 "VIN")
+			(pinfunction "Pin_1")
+			(pintype "passive")
+		)
+		(pad "1" thru_hole circle
 			(at 0 0)
 			(size 2.2 2.2)
@@
 	)
 	(gr_text "VIN"
-		(at 105.42 110.6 270)
+		(at 109.3 116.8 0)
 		(layer "B.SilkS")
 		(effects

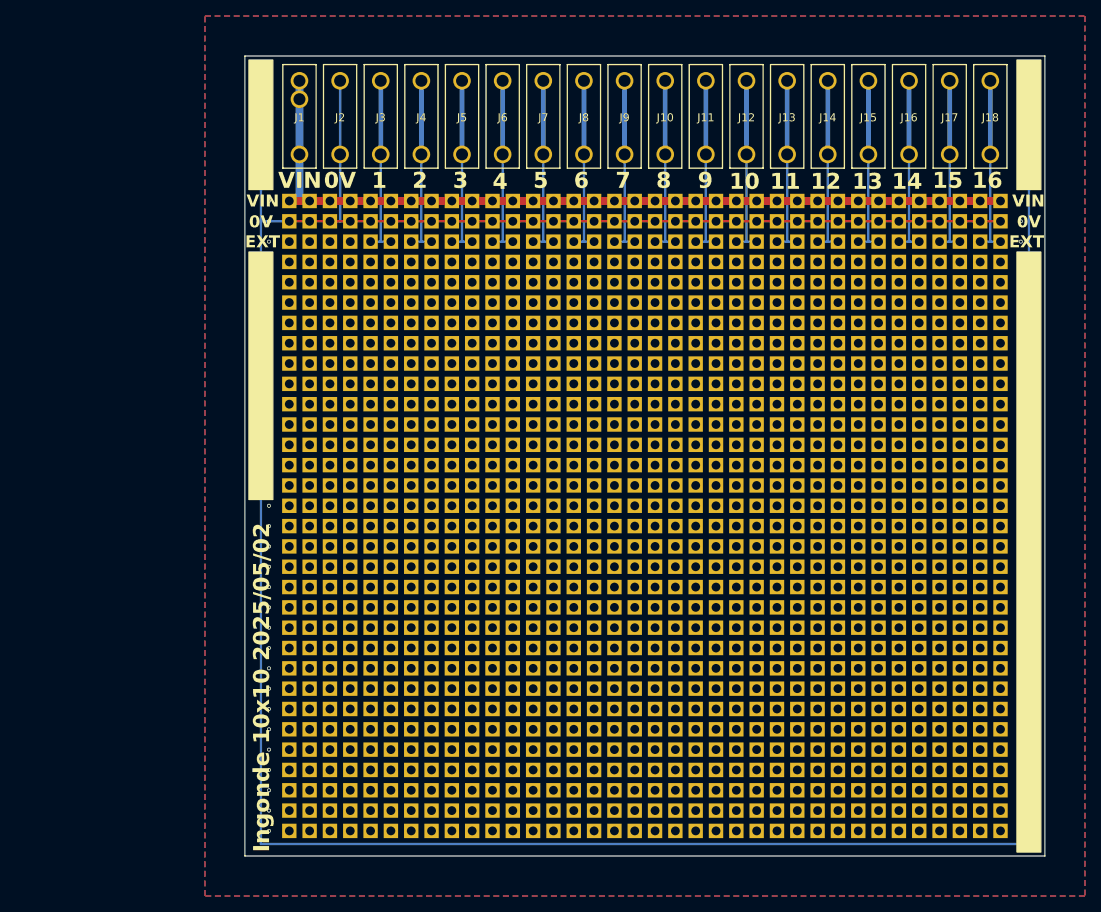
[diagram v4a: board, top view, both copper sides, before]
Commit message: Ingonde_10x10: fabrication
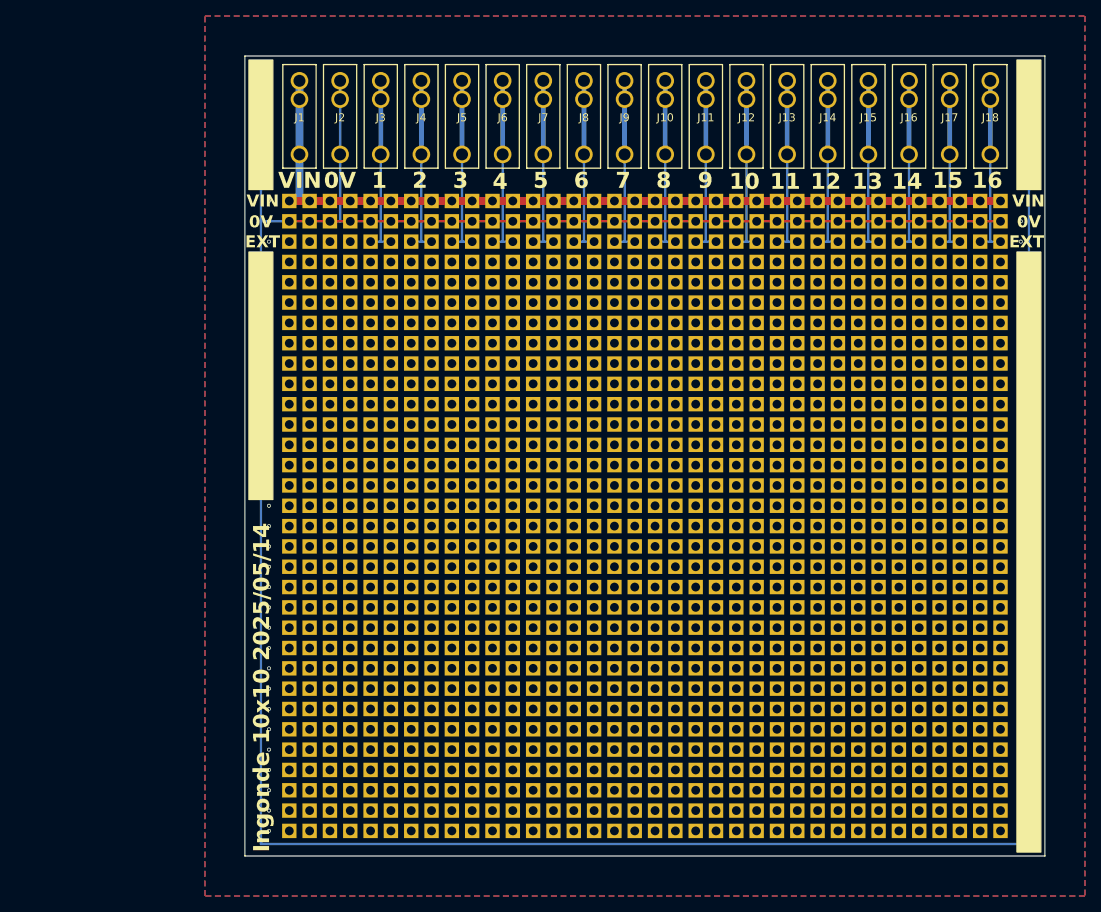
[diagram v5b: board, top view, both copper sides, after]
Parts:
- J10, J11, J12, J13, J14, J15, J16, J17, J18, J2, J3, J4, J5, J6, J7, J8, J9: footprint Chimere_comps:CONN_2060-1451_998-404_WAGO -> Chimere_comps:Conn_bornier_et_wago
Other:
- board text added: "Ingonde 10x10 2025/05/14"
- board text removed: "Ingonde 10x10 2025/05/02"
